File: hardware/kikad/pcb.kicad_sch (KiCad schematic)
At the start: 22 parts, among them J1 LED, J2 BOARD

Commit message: version 0.2
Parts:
- removed D5: LED_RKGB, LED_THT:LED_D5.0mm-4_RGB_Wide_Pins, symbol Device:LED_RKGB
- removed J1: LED, Connector_PinSocket_2.54mm:PinSocket_1x06_P2.54mm_Vertical, symbol Connector:Conn_01x06_Pin
- added D7: LED_Dual_AKA, Connector_JST:JST_XH_B3B-XH-A_1x03_P2.50mm_Vertical, symbol Device:LED_Dual_AKA
- U1: footprint esp_32_c3_supper_mini:esp_32_c3_supper_mini -> esp_32_c3_supper_mini:esp_32_c3_supper_mini_tht_smd
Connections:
- net GND: now also D7.2 (K)
- net at R14.2: now also D7.3 (A2); no longer U1.9 (GPIO5)
- net at R13.1: now also D7.1 (A1); no longer U1.10 (GPIO6)
- net at R14.1: now also U1.9 (GPIO5)
- net at R13.2: now also U1.10 (GPIO6)
- no-connect marks 11 -> 10
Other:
- moved on the sheet: R13, R14

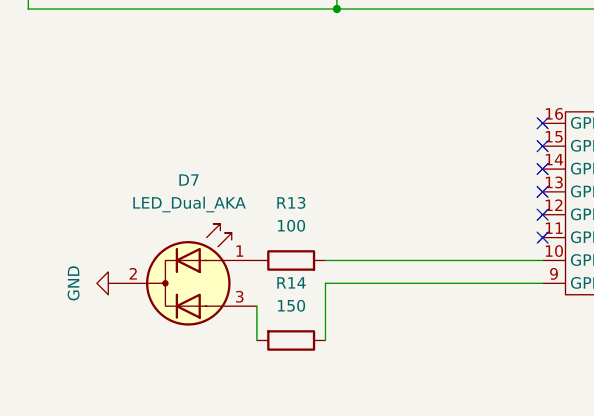
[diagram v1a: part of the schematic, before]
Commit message: works nfc reader
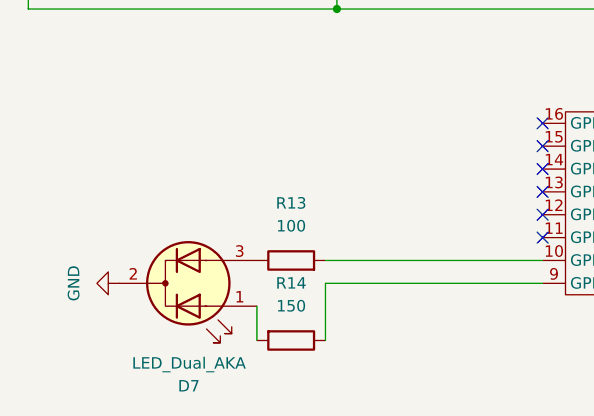
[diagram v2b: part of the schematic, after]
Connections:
- net at D7.1 (A1): now also R14.2; no longer R13.1
- net at D7.3 (A2): now also R13.1; no longer R14.2
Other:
- moved on the sheet: D7
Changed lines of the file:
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@@
 		(lib_id "Device:LED_Dual_AKA")
 		(at 38.1 86.36 0)
+		(mirror x)
 		(unit 1)
 		(exclude_from_sim no)
@@
 		(on_board yes)
 		(dnp no)
-		(fields_autoplaced yes)
 		(property "Reference" "D7"
-			(at 38.1635 74.93 0)
+			(at 38.1635 97.79 0)
 			(effects
 				(font
@@
 		)
 		(property "Value" "LED_Dual_AKA"
-			(at 38.1635 77.47 0)
+			(at 38.1635 95.25 0)
 			(effects
 				(font

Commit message: make the v0.3 read to use
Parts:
- removed D7: LED_Dual_AKA, Connector_JST:JST_XH_B3B-XH-A_1x03_P2.50mm_Vertical, symbol Device:LED_Dual_AKA
- removed J2: BOARD, Connector_PinSocket_2.54mm:PinSocket_1x02_P2.54mm_Vertical, symbol Connector:Conn_01x02_Pin
- added BZ1: Buzzer, Buzzer_Beeper:MagneticBuzzer_ProSignal_ABI-010-RC, symbol Device:Buzzer
- added J1: Output, Connector_JST:JST_XH_B3B-XH-A_1x03_P2.50mm_Vertical, symbol Connector:Conn_01x03_Pin
- added U2: ~, esp_32_c3_supper_mini:PN532 NFC RFID, symbol esp_c3_32_supper_mini:PN532_NFC_RFID_module_V3
- R14: value 150 -> 0
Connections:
- net B: now also U1.16 (GPIO21); no longer U1.7 (GPIO1)
- net G: now also U1.15 (GPIO20); no longer U1.6 (GPIO2)
- net GND: now also BZ1.2 (-), J1.1 (Pin_1), U2.10 (GND)
- net R: now also U1.14 (GPIO10); no longer U1.5 (GPIO3)
- net at R14.2: now also U1.3 (3V3)
- net at R13.1: now also U1.13 (GPIO9/SCL)
- net at U1.10 (GPIO6/MOSI): now also U2.7 (MOSI); no longer R13.2
- net at U1.11 (GPIO7/SS): now also U2.8 (SS)
- net at U1.12 (GPIO8/SDA): now also U2.12 (RSTO)
- net at U1.4 (GPIO4/SCK): now also U2.5 (SCK)
- net at U1.9 (GPIO5/MISO): now also U2.6 (MISO); no longer R14.1
- new net: R14.1, U2.9 (VCC)
- new net: BZ1.1 (+), R13.2
- new net: J1.3 (Pin_3), U1.6 (GPIO2)
- new net: J1.2 (Pin_2), U1.7 (GPIO1)
- no-connect marks 10 -> 8
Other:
- moved on the sheet: D1, D2, D3, D4, R1, R10, R11, R12, R2, R3, R4, R5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

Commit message: implement binary build
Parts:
- D1, D2, D3, D4: footprint LED_THT:LED_D5.0mm-4_RGB_Wide_Pins -> LED_THT:LED_D5.0mm-4_RGB_Wide_Pins_CNC_read
- R1, R10, R11, R12, R13, R14, R2, R3, R4, R5, R6, R7, R8, R9: footprint Resistor_THT:R_Axial_DIN0204_L3.6mm_D1.6mm_P7.62mm_Horizontal -> Resistor_THT:CNC_Ready_R_Axial_DIN0204_L3.6mm_D1.6mm_P7.62mm_Horizontal
- U2: footprint esp_32_c3_supper_mini:PN532 NFC RFID -> esp_32_c3_supper_mini:PN532 NFC RFID simple (one row)
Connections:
- net B: now also U1.15 (GPIO20); no longer U1.16 (GPIO21)
- net G: now also U1.14 (GPIO10); no longer U1.15 (GPIO20)
- net R: now also U1.13 (GPIO9/SCL); no longer U1.14 (GPIO10)
- net at R13.1: now also U1.16 (GPIO21); no longer U1.13 (GPIO9/SCL)
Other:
- moved on the sheet: D1, D2, D3, D4, R1, R10, R11, R12, R2, R3, R4, R5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

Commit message: update the buzzer pin
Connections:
- net at R13.1: now also U1.5 (GPIO3); no longer U1.16 (GPIO21)
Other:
- moved on the sheet: BZ1, R13
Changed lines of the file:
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@@
 	)
 	(no_connect
-		(at 73.66 80.01)
+		(at 105.41 87.63)
 	)
 	(no_connect
@@
 	(wire
 		(pts
+			(xy 52.07 80.01) (xy 73.66 80.01)
+		)
+		(stroke
+			(width 0)
+			(type default)
+		)
+	)
+	(wire
+		(pts
 			(xy 246.38 63.5) (xy 246.38 67.31)
 		)
@@
 	(wire
 		(pts
-			(xy 113.03 87.63) (xy 105.41 87.63)
-		)
-		(stroke
-			(width 0)
-			(type default)
-		)
-	)
-	(wire
-		(pts
 			(xy 198.12 63.5) (xy 194.31 63.5)
 		)
@@
 		(pts
 			(xy 101.6 57.15) (xy 101.6 48.26)
-		)
-		(stroke
-			(width 0)
-			(type default)
-		)
-	)
-	(wire
-		(pts
-			(xy 113.03 93.98) (xy 113.03 87.63)
 		)
 		(stroke
@@
 	(symbol
 		(lib_id "Device:R")
-		(at 113.03 97.79 0)
+		(at 48.26 80.01 270)
 		(unit 1)
 		(exclude_from_sim no)
@@
 		(fields_autoplaced yes)
 		(property "Reference" "R13"
-			(at 119.38 97.79 90)
+			(at 48.26 86.36 90)
 			(effects
 				(font
@@
 		)
 		(property "Value" "100"
-			(at 116.84 97.79 90)
+			(at 48.26 83.82 90)
 			(effects
 				(font
@@
 		)
 		(property "Footprint" "Resistor_THT:CNC_Ready_R_Axial_DIN0204_L3.6mm_D1.6mm_P7.62mm_Horizontal"
-			(at 111.252 97.79 90)
+			(at 48.26 78.232 90)
 			(effects
 				(font
@@
 		)
 		(property "Datasheet" "~"
-			(at 113.03 97.79 0)
+			(at 48.26 80.01 0)
 			(effects
 				(font
@@
 		)
 		(property "Description" "Resistor"
-			(at 113.03 97.79 0)
+			(at 48.26 80.01 0)
 			(effects
 				(font
@@
 	(symbol
 		(lib_id "power:GND")
-		(at 107.95 101.6 180)
+		(at 44.45 74.93 90)
 		(unit 1)
 		(exclude_from_sim no)
@@
 		(fields_autoplaced yes)
 		(property "Reference" "#PWR08"
-			(at 107.95 95.25 0)
+			(at 50.8 74.93 0)
 			(effects
 				(font
@@
 		)
 		(property "Value" "GND"
-			(at 107.95 96.52 0)
+			(at 49.53 74.93 0)
 			(effects
 				(font
@@
 		)
 		(property "Footprint" ""
-			(at 107.95 101.6 0)
+			(at 44.45 74.93 0)
 			(effects
 				(font
@@
 		)
 		(property "Datasheet" ""
-			(at 107.95 101.6 0)
+			(at 44.45 74.93 0)
 			(effects
 				(font
@@
 		)
 		(property "Description" "Power symbol creates a global label with name \"GND\" , ground"
-			(at 107.95 101.6 0)
+			(at 44.45 74.93 0)
 			(effects
 				(font
@@
 	(symbol
 		(lib_id "Device:Buzzer")
-		(at 110.49 104.14 270)
+		(at 41.91 77.47 180)
 		(unit 1)
 		(exclude_from_sim no)
@@
 		(fields_autoplaced yes)
 		(property "Reference" "BZ1"
-			(at 111.7601 107.95 0)
+			(at 38.1 78.7401 0)
 			(effects
 				(font
@@
 		)
 		(property "Value" "Buzzer"
-			(at 109.2201 107.95 0)
+			(at 38.1 76.2001 0)
 			(effects
 				(font
@@
 		)
 		(property "Footprint" "Buzzer_Beeper:MagneticBuzzer_ProSignal_ABI-010-RC"
-			(at 113.03 103.505 90)
+			(at 42.545 80.01 90)
 			(effects
 				(font
@@
 		)
 		(property "Datasheet" "~"
-			(at 113.03 103.505 90)
+			(at 42.545 80.01 90)
 			(effects
 				(font
@@
 		)
 		(property "Description" "Buzzer, polarized"
-			(at 110.49 104.14 0)
-			(effects
-				(font
+			(at 41.91 77.47 0)
+			(effects
+				(font

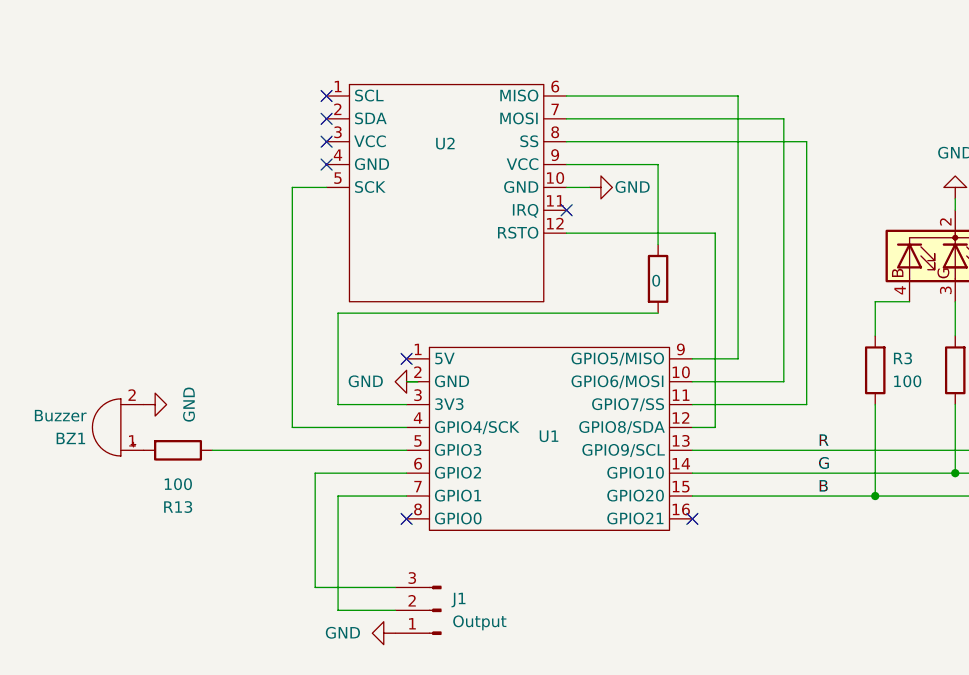
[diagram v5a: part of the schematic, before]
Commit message: update the kikad pcb, move buzzer to GPIO0
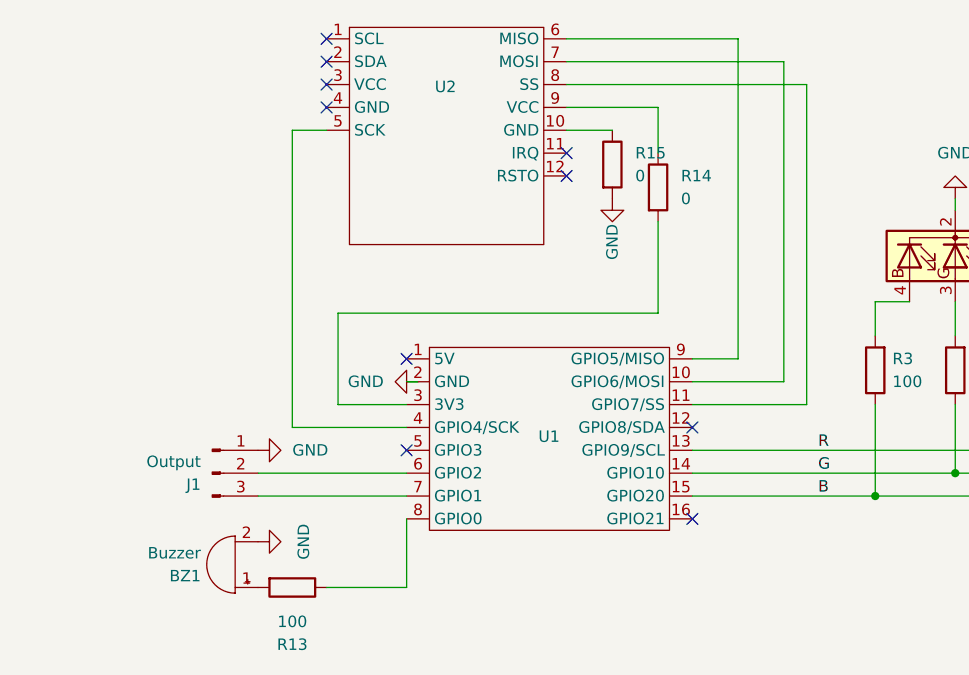
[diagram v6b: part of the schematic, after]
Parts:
- added R15: 0, Resistor_THT:CNC_Ready_R_Axial_DIN0204_L3.6mm_D1.6mm_P7.62mm_Horizontal, symbol Device:R
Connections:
- net GND: now also R15.2; no longer U2.10 (GND)
- net at U2.12 (RSTO): no longer U1.12 (GPIO8/SDA)
- net at R13.1: now also U1.8 (GPIO0); no longer U1.5 (GPIO3)
- net at U1.6 (GPIO2): now also J1.2 (Pin_2); no longer J1.3 (Pin_3)
- net at U1.7 (GPIO1): now also J1.3 (Pin_3); no longer J1.2 (Pin_2)
- new net: R15.1, U2.10 (GND)
- no-connect marks 8 -> 10
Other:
- moved on the sheet: BZ1, J1, R13, U2

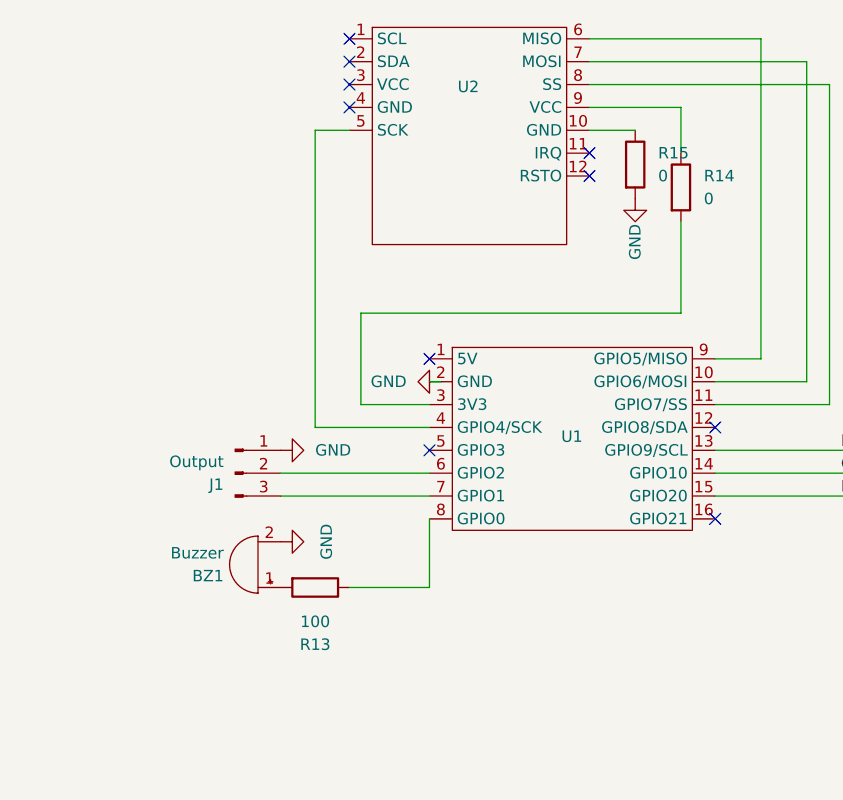
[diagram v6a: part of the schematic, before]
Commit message: ad power for 5v esp
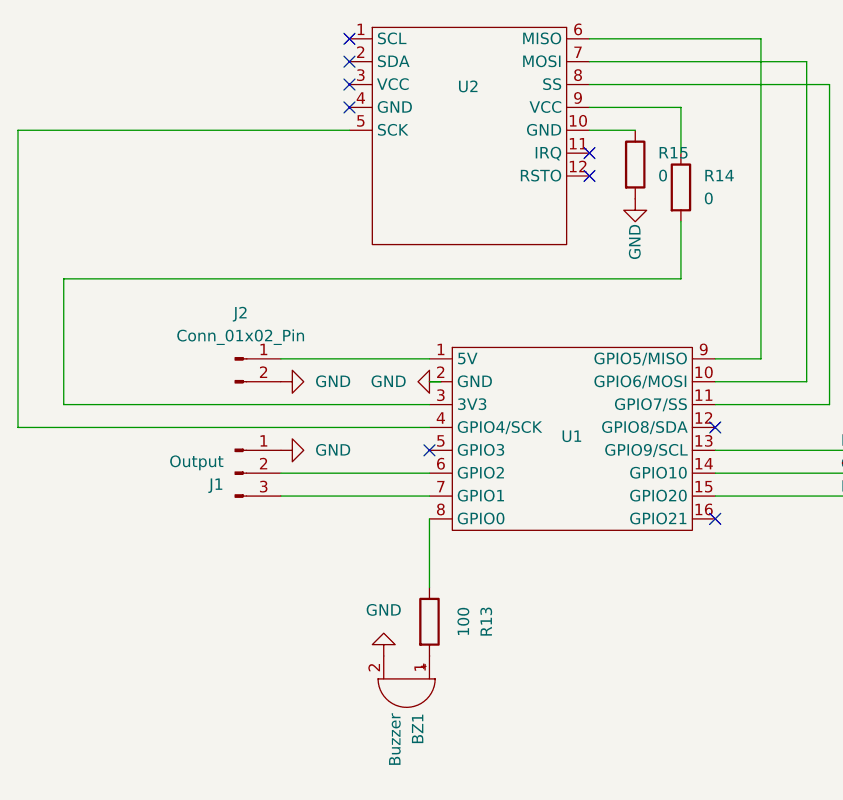
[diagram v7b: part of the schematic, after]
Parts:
- added J2: Conn_01x02_Pin, Connector_JST:JST_EH_B2B-EH-A_1x02_P2.50mm_Vertical, symbol Connector:Conn_01x02_Pin
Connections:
- net GND: now also J2.2 (Pin_2)
- net at U1.1 (5V): now also J2.1 (Pin_1)
- no-connect marks 10 -> 9
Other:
- moved on the sheet: BZ1, R13
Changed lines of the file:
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@@
-	)
-	(no_connect
-		(at 73.66 69.85)
 	)
 	(no_connect
@@
 	(wire
 		(pts
-			(xy 60.96 77.47) (xy 73.66 77.47)
+			(xy 27.94 77.47) (xy 73.66 77.47)
 		)
 		(stroke
@@
 	(wire
 		(pts
-			(xy 66.04 74.93) (xy 73.66 74.93)
+			(xy 33.02 74.93) (xy 73.66 74.93)
 		)
 		(stroke
@@
 	(wire
 		(pts
-			(xy 60.96 44.45) (xy 60.96 77.47)
-		)
-		(stroke
-			(width 0)
-			(type default)
-		)
-	)
-	(wire
-		(pts
-			(xy 73.66 95.25) (xy 64.77 95.25)
+			(xy 27.94 44.45) (xy 27.94 77.47)
 		)
 		(stroke
@@
 	(wire
 		(pts
+			(xy 101.6 54.61) (xy 101.6 60.96)
+		)
+		(stroke
+			(width 0)
+			(type default)
+		)
+	)
+	(wire
+		(pts
 			(xy 57.15 85.09) (xy 73.66 85.09)
 		)
@@
 	(wire
 		(pts
-			(xy 101.6 54.61) (xy 101.6 64.77)
-		)
-		(stroke
-			(width 0)
-			(type default)
-		)
-	)
-	(wire
-		(pts
 			(xy 73.66 87.63) (xy 73.66 95.25)
 		)
@@
 	(wire
 		(pts
-			(xy 66.04 64.77) (xy 66.04 74.93)
+			(xy 33.02 60.96) (xy 33.02 74.93)
 		)
 		(stroke
@@
 	(wire
 		(pts
-			(xy 101.6 64.77) (xy 66.04 64.77)
-		)
-		(stroke
-			(width 0)
-			(type default)
-		)
-	)
-	(wire
-		(pts
 			(xy 143.51 74.93) (xy 143.51 80.01)
 		)
@@
 	(wire
 		(pts
-			(xy 64.77 44.45) (xy 60.96 44.45)
+			(xy 64.77 44.45) (xy 27.94 44.45)
 		)
 		(stroke
@@
 	(wire
 		(pts
+			(xy 57.15 69.85) (xy 73.66 69.85)
+		)
+		(stroke
+			(width 0)
+			(type default)
+		)
+	)
+	(wire
+		(pts
 			(xy 143.51 63.5) (xy 143.51 67.31)
 		)
@@
 		(pts
 			(xy 101.6 41.91) (xy 91.44 41.91)
+		)
+		(stroke
+			(width 0)
+			(type default)
+		)
+	)
+	(wire
+		(pts
+			(xy 101.6 60.96) (xy 33.02 60.96)
 		)
 		(stroke
@@
 	(symbol
 		(lib_id "Device:R")
-		(at 60.96 95.25 270)
+		(at 73.66 99.06 0)
 		(unit 1)
 		(exclude_from_sim no)
@@
 		(fields_autoplaced yes)
 		(property "Reference" "R13"
-			(at 60.96 101.6 90)
+			(at 80.01 99.06 90)
 			(effects
 				(font
@@
 		)
 		(property "Value" "100"
-			(at 60.96 99.06 90)
+			(at 77.47 99.06 90)
 			(effects
 				(font
@@
 		)
 		(property "Footprint" "Resistor_THT:CNC_Ready_R_Axial_DIN0204_L3.6mm_D1.6mm_P7.62mm_Horizontal"
-			(at 60.96 93.472 90)
+			(at 71.882 99.06 90)
 			(effects
 				(font
@@
 		)
 		(property "Datasheet" "~"
-			(at 60.96 95.25 0)
+			(at 73.66 99.06 0)
 			(effects
 				(font
@@
 		)
 		(property "Description" "Resistor"
-			(at 60.96 95.25 0)
+			(at 73.66 99.06 0)
 			(effects
 				(font
@@
 	(symbol
 		(lib_id "power:GND")
-		(at 57.15 90.17 90)
+		(at 68.58 102.87 180)
 		(unit 1)
 		(exclude_from_sim no)
@@
 		(fields_autoplaced yes)
 		(property "Reference" "#PWR08"
-			(at 63.5 90.17 0)
+			(at 68.58 96.52 0)
 			(effects
 				(font
@@
 		)
 		(property "Value" "GND"
-			(at 62.23 90.17 0)
+			(at 68.58 97.79 0)
 			(effects
 				(font
@@
 		)
 		(property "Footprint" ""
-			(at 57.15 90.17 0)
+			(at 68.58 102.87 0)
 			(effects
 				(font
@@
 		)
 		(property "Datasheet" ""
-			(at 57.15 90.17 0)
+			(at 68.58 102.87 0)
 			(effects
 				(font
@@
 		)
 		(property "Description" "Power symbol creates a global label with name \"GND\" , ground"
-			(at 57.15 90.17 0)
+			(at 68.58 102.87 0)
 			(effects
 				(font
@@
 	)
 	(symbol
+		(lib_id "Connector:Conn_01x02_Pin")
+		(at 52.07 69.85 0)
+		(unit 1)
+		(exclude_from_sim no)
+		(in_bom yes)
+		(on_board yes)
+		(dnp no)
+		(fields_autoplaced yes)
+		(property "Reference" "J2"
+			(at 52.705 64.77 0)
+			(effects
+				(font
+					(size 1.27 1.27)
+				)
+			)
+		)
+		(property "Value" "Conn_01x02_Pin"
+			(at 52.705 67.31 0)
+			(effects
+				(font
+					(size 1.27 1.27)
+				)
+			)
+		)
+		(property "Footprint" "Connector_JST:JST_EH_B2B-EH-A_1x02_P2.50mm_Vertical"
+			(at 52.07 69.85 0)
+			(effects
+				(font
+					(size 1.27 1.27)
+				)
+				(hide yes)
+			)
+		)
+		(property "Datasheet" "~"
+			(at 52.07 69.85 0)
+			(effects
+				(font
+					(size 1.27 1.27)
+				)
+				(hide yes)
+			)
+		)
+		(property "Description" "Generic connector, single row, 01x02, script generated"
+			(at 52.07 69.85 0)
+			(effects
+				(font
+					(size 1.27 1.27)
+				)
+				(hide yes)
+			)
+		)
+		(pin "2"
+		)
+		(pin "1"
+		)
+		(instances
+			(project ""
+				(path "/e0f69ff1-e3b8-4d01-8d2a-72fcb9b35158"
+					(reference "J2")
+					(unit 1)
+				)
+			)
+		)
+	)
+	(symbol
 		(lib_id "power:GND")
 		(at 203.2 52.07 180)
@@
 	(symbol
 		(lib_id "power:GND")
+		(at 57.15 72.39 90)
+		(unit 1)
+		(exclude_from_sim no)
+		(in_bom yes)
+		(on_board yes)
+		(dnp no)
+		(fields_autoplaced yes)
+		(property "Reference" "#PWR09"
+			(at 63.5 72.39 0)
+			(effects
+				(font
+					(size 1.27 1.27)
+				)
+				(hide yes)
+			)
+		)
+		(property "Value" "GND"
+			(at 60.96 72.3899 90)
+			(effects
+				(font
+					(size 1.27 1.27)
+				)
+				(justify right)
+			)
+		)
+		(property "Footprint" ""
+			(at 57.15 72.39 0)
+			(effects
+				(font
+					(size 1.27 1.27)
+				)
+				(hide yes)
+			)
+		)
+		(property "Datasheet" ""
+			(at 57.15 72.39 0)
+			(effects
+				(font
+					(size 1.27 1.27)
+				)
+				(hide yes)
+			)
+		)
+		(property "Description" "Power symbol creates a global label with name \"GND\" , ground"
+			(at 57.15 72.39 0)
+			(effects
+				(font
+					(size 1.27 1.27)
+				)
+				(hide yes)
+			)
+		)
+		(pin "1"
+		)
+		(instances
+			(project ""
+				(path "/e0f69ff1-e3b8-4d01-8d2a-72fcb9b35158"
+					(reference "#PWR09")
+					(unit 1)
+				)
+			)
+		)
+	)
+	(symbol
+		(lib_id "power:GND")
 		(at 237.49 52.07 180)
 		(unit 1)
@@
 	(symbol
 		(lib_id "Device:Buzzer")
-		(at 54.61 92.71 180)
+		(at 71.12 105.41 270)
 		(unit 1)
 		(exclude_from_sim no)
@@
 		(fields_autoplaced yes)
 		(property "Reference" "BZ1"
-			(at 50.8 93.9801 0)
+			(at 72.3901 109.22 0)
 			(effects
 				(font
@@
 		)
 		(property "Value" "Buzzer"
-			(at 50.8 91.4401 0)
+			(at 69.8501 109.22 0)
 			(effects
 				(font
@@
 		)
 		(property "Footprint" "Buzzer_Beeper:MagneticBuzzer_ProSignal_ABI-010-RC"
-			(at 55.245 95.25 90)
+			(at 73.66 104.775 90)
 			(effects
 				(font
@@
 		)
 		(property "Datasheet" "~"
-			(at 55.245 95.25 90)
+			(at 73.66 104.775 90)
 			(effects
 				(font
@@
 		)
 		(property "Description" "Buzzer, polarized"
-			(at 54.61 92.71 0)
-			(effects
-				(font
+			(at 71.12 105.41 0)
+			(effects
+				(font
